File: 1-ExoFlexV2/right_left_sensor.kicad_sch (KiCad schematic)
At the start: 20 parts, among them U30 SN74LVC3G14DCUT_V2, U31 SN74LVC3G14DCUT_V2, U32 SN74LVC1G08DBVR, U33 SN74LVC3G14DCUT_V2, U34 SN74LVC3G14DCUT_V2, U35 SN74LVC1G08DBVR, U36 SN74LVC1G32DBVR

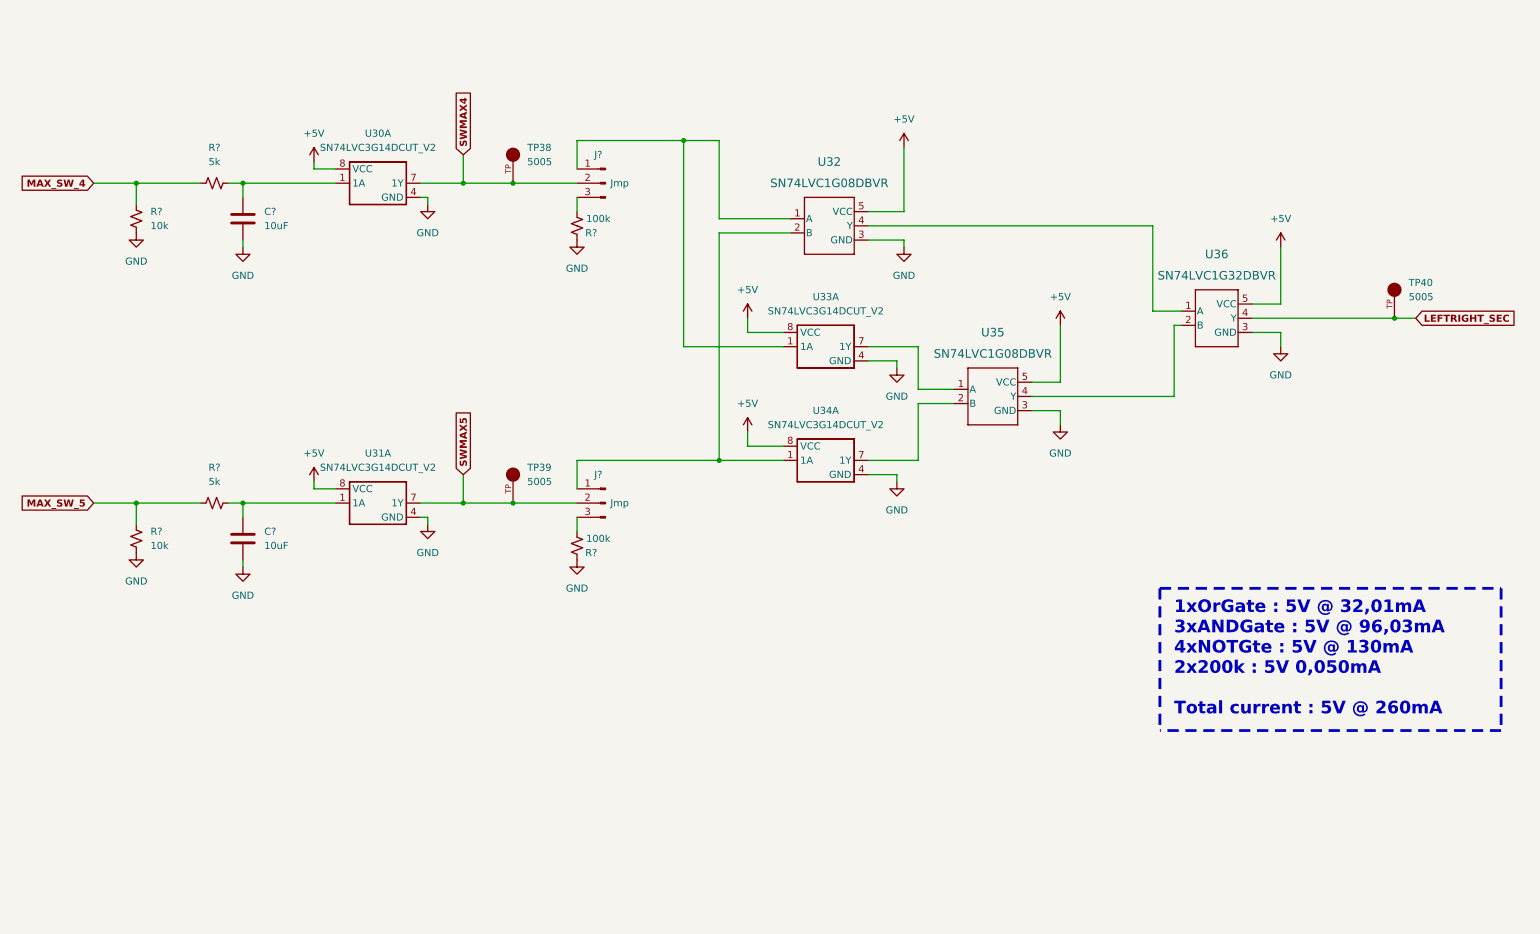
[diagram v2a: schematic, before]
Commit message: Test points et notes
- Ajout de tous les tests point nécessaires
-  Ajoute des sections de notes dans chaque page
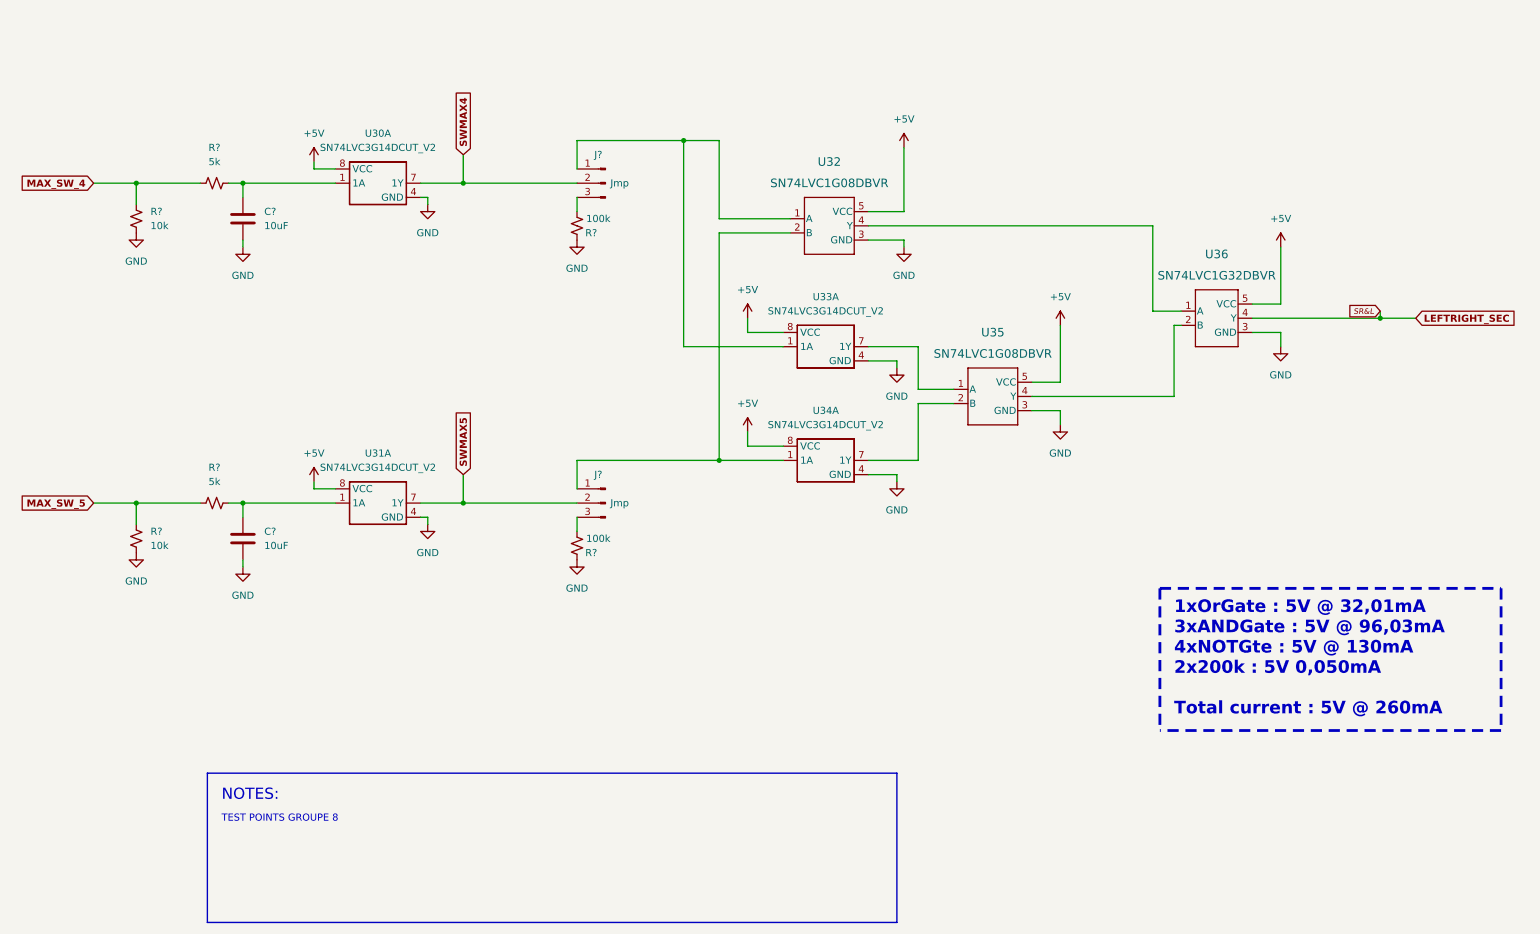
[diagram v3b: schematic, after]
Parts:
- removed TP38, TP39, TP40: 5005, FootPrint:KEYSTONE_5005, symbol SymLib:5005
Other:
- note added: "NOTES:"
- note added: "TEST POINTS GROUPE 8"
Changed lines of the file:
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@@
   (junction (at 96.52 120.65) (diameter 0) (color 0 0 0 0)
   )
-  (junction (at 105.41 63.5) (diameter 0) (color 0 0 0 0)
-  )
   (junction (at 38.1 63.5) (diameter 0) (color 0 0 0 0)
   )
-  (junction (at 262.89 87.63) (diameter 0) (color 0 0 0 0)
+  (junction (at 260.35 87.63) (diameter 0) (color 0 0 0 0)
   )
   (junction (at 135.89 55.88) (diameter 0) (color 0 0 0 0)
   )
-  (junction (at 105.41 120.65) (diameter 0) (color 0 0 0 0)
-  )
   (junction (at 38.1 120.65) (diameter 0) (color 0 0 0 0)
   )
@@
     (stroke (width 0) (type default) (color 0 0 0 0))
   )
-  (wire (pts (xy 96.52 120.65) (xy 105.41 120.65))
+  (wire (pts (xy 96.52 120.65) (xy 116.84 120.65))
     (stroke (width 0) (type default) (color 0 0 0 0))
   )
@@
     (stroke (width 0.5) (type dash) (color 255 148 44 1))
   )
+  (polyline (pts (xy 173.99 195.58) (xy 50.8 195.58))
+    (stroke (width 0.25) (type solid) (color 0 0 0 0))
+  )
   (wire (pts (xy 242.57 85.09) (xy 237.49 85.09))
     (stroke (width 0) (type default) (color 0 0 0 0))
@@
     (stroke (width 0) (type default) (color 0 0 0 0))
   )
-  (wire (pts (xy 105.41 120.65) (xy 116.84 120.65))
-    (stroke (width 0) (type default) (color 0 0 0 0))
-  )
   (wire (pts (xy 135.89 55.88) (xy 135.89 92.71))
     (stroke (width 0) (type default) (color 0 0 0 0))
   )
   (wire (pts (xy 57.15 130.81) (xy 57.15 132.08))
-    (stroke (width 0) (type default) (color 0 0 0 0))
-  )
-  (wire (pts (xy 105.41 63.5) (xy 116.84 63.5))
     (stroke (width 0) (type default) (color 0 0 0 0))
   )
@@
     (stroke (width 0.5) (type dash) (color 255 148 44 1))
   )
+  (polyline (pts (xy 50.8 168.91) (xy 50.8 195.58))
+    (stroke (width 0.25) (type solid) (color 0 0 0 0))
+  )
   (wire (pts (xy 90.17 67.31) (xy 90.17 66.04))
     (stroke (width 0) (type default) (color 0 0 0 0))
@@
     (stroke (width 0) (type default) (color 0 0 0 0))
   )
-  (wire (pts (xy 96.52 63.5) (xy 105.41 63.5))
+  (wire (pts (xy 96.52 63.5) (xy 116.84 63.5))
     (stroke (width 0) (type default) (color 0 0 0 0))
   )
@@
     (stroke (width 0) (type default) (color 0 0 0 0))
   )
+  (polyline (pts (xy 50.8 168.91) (xy 173.99 168.91))
+    (stroke (width 0.25) (type solid) (color 0 0 0 0))
+  )
   (wire (pts (xy 57.15 120.65) (xy 73.66 120.65))
     (stroke (width 0) (type default) (color 0 0 0 0))
@@
     (stroke (width 0) (type default) (color 0 0 0 0))
   )
+  (wire (pts (xy 260.35 86.36) (xy 260.35 87.63))
+    (stroke (width 0) (type default) (color 0 0 0 0))
+  )
   (wire (pts (xy 116.84 113.03) (xy 142.24 113.03))
     (stroke (width 0) (type default) (color 0 0 0 0))
@@
     (stroke (width 0) (type default) (color 0 0 0 0))
   )
+  (polyline (pts (xy 173.99 168.91) (xy 173.99 195.58))
+    (stroke (width 0.25) (type solid) (color 0 0 0 0))
+  )
   (wire (pts (xy 73.66 118.11) (xy 69.85 118.11))
     (stroke (width 0) (type default) (color 0 0 0 0))
   )
-  (wire (pts (xy 237.49 87.63) (xy 262.89 87.63))
+  (wire (pts (xy 237.49 87.63) (xy 260.35 87.63))
     (stroke (width 0) (type default) (color 0 0 0 0))
   )
@@
     (stroke (width 0) (type default) (color 0 0 0 0))
   )
-  (wire (pts (xy 262.89 87.63) (xy 266.7 87.63))
-    (stroke (width 0) (type default) (color 0 0 0 0))
+  (wire (pts (xy 260.35 87.63) (xy 266.7 87.63))
+    (stroke (width 0) (type default) (color 0 0 0 0))
+  )
+  (text "NOTES:" (at 53.34 173.99 0)
+    (effects (font (size 2 2)) (justify left bottom))
   )
   (text "1xOrGate : 5V @ 32,01mA\n3xANDGate : 5V @ 96,03mA\n4xNOTGte : 5V @ 130mA\n2x200k : 5V 0,050mA\n\nTotal current : 5V @ 260mA"
     (at 223.52 158.75 0)
     (effects (font (size 2.25 2.25) (thickness 0.5) bold) (justify left bottom))
+  )
+  (text "TEST POINTS GROUPE 8" (at 53.34 177.8 0)
+    (effects (font (size 1.27 1.27)) (justify left bottom))
   )
   (global_label "MAX_SW_5" (shape input) (at 30.48 120.65 180) (fields_autoplaced)
@@
     )
   )
+  (global_label "SR&L" (shape input) (at 260.35 86.36 180) (fields_autoplaced)
+    (effects (font (size 1 1) italic) (justify right))
+    (property "Intersheet References" "${INTERSHEET_REFS}" (id 0) (at 254.0987 86.2975 0)
+      (effects (font (size 1 1) italic) (justify right) hide)
+    )
+  )
   (global_label "SWMAX5" (shape input) (at 96.52 115.57 90) (fields_autoplaced)
     (effects (font (size 1.27 1.27) (thickness 0.254) bold) (justify left))
@@
     )
   )
-  (symbol (lib_id "SymLib:5005") (at 105.41 58.42 90) (unit 1)
-    (in_bom yes) (on_board yes) (fields_autoplaced)
-    (property "Reference" "TP38" (id 0) (at 107.95 57.1499 90)
-      (effects (font (size 1.27 1.27)) (justify right))
-    )
-    (property "Value" "5005" (id 1) (at 107.95 59.6899 90)
-      (effects (font (size 1.27 1.27)) (justify right))
-    )
-    (property "Footprint" "FootPrint:KEYSTONE_5005" (id 2) (at 105.41 58.42 0)
-      (effects (font (size 1.27 1.27)) (justify bottom) hide)
-    )
-    (property "Datasheet" "" (id 3) (at 105.41 58.42 0)
-      (effects (font (size 1.27 1.27)) hide)
-    )
-    (property "MF" "Keystone Electronics" (id 4) (at 105.41 58.42 0)
-      (effects (font (size 1.27 1.27)) (justify bottom) hide)
-    )
-    (property "DESCRIPTION" "Compact THM Test Point -Red" (id 5) (at 105.41 58.42 0)
-      (effects (font (size 1.27 1.27)) (justify bottom) hide)
-    )
-    (property "PACKAGE" "NON STANDARD-1 Keystone" (id 6) (at 105.41 58.42 0)
-      (effects (font (size 1.27 1.27)) (justify bottom) hide)
-    )
-    (property "PRICE" "None" (id 7) (at 105.41 58.42 0)
-      (effects (font (size 1.27 1.27)) (justify bottom) hide)
-    )
-    (property "MP" "5005" (id 8) (at 105.41 58.42 0)
-      (effects (font (size 1.27 1.27)) (justify bottom) hide)
-    )
-    (property "AVAILABILITY" "In Stock" (id 9) (at 105.41 58.42 0)
-      (effects (font (size 1.27 1.27)) (justify bottom) hide)
-    )
-    (property "PURCHASE-URL" "https://pricing.snapeda.com/search/part/5005/?ref=eda" (id 10) (at 105.41 58.42 0)
-      (effects (font (size 1.27 1.27)) (justify bottom) hide)
-    )
-    (pin "TP")
-  )
   (symbol (lib_id "Device:C") (at 57.15 127 0) (unit 1)
     (in_bom yes) (on_board yes) (fields_autoplaced)
@@
     )
     (pin "1")
-  )
-  (symbol (lib_id "SymLib:5005") (at 105.41 115.57 90) (unit 1)
-    (in_bom yes) (on_board yes) (fields_autoplaced)
-    (property "Reference" "TP39" (id 0) (at 107.95 114.2999 90)
-      (effects (font (size 1.27 1.27)) (justify right))
-    )
-    (property "Value" "5005" (id 1) (at 107.95 116.8399 90)
-      (effects (font (size 1.27 1.27)) (justify right))
-    )
-    (property "Footprint" "FootPrint:KEYSTONE_5005" (id 2) (at 105.41 115.57 0)
-      (effects (font (size 1.27 1.27)) (justify bottom) hide)
-    )
-    (property "Datasheet" "" (id 3) (at 105.41 115.57 0)
-      (effects (font (size 1.27 1.27)) hide)
-    )
-    (property "MF" "Keystone Electronics" (id 4) (at 105.41 115.57 0)
-      (effects (font (size 1.27 1.27)) (justify bottom) hide)
-    )
-    (property "DESCRIPTION" "Compact THM Test Point -Red" (id 5) (at 105.41 115.57 0)
-      (effects (font (size 1.27 1.27)) (justify bottom) hide)
-    )
-    (property "PACKAGE" "NON STANDARD-1 Keystone" (id 6) (at 105.41 115.57 0)
-      (effects (font (size 1.27 1.27)) (justify bottom) hide)
-    )
-    (property "PRICE" "None" (id 7) (at 105.41 115.57 0)
-      (effects (font (size 1.27 1.27)) (justify bottom) hide)
-    )
-    (property "MP" "5005" (id 8) (at 105.41 115.57 0)
-      (effects (font (size 1.27 1.27)) (justify bottom) hide)
-    )
-    (property "AVAILABILITY" "In Stock" (id 9) (at 105.41 115.57 0)
-      (effects (font (size 1.27 1.27)) (justify bottom) hide)
-    )
-    (property "PURCHASE-URL" "https://pricing.snapeda.com/search/part/5005/?ref=eda" (id 10) (at 105.41 115.57 0)
-      (effects (font (size 1.27 1.27)) (justify bottom) hide)
-    )
-    (pin "TP")
   )
   (symbol (lib_id "SymLib:SN74LVC1G08DBVR") (at 137.16 68.58 0) (unit 1)
@@
     (pin "2")
   )
-  (symbol (lib_id "SymLib:5005") (at 262.89 82.55 90) (unit 1)
-    (in_bom yes) (on_board yes) (fields_autoplaced)
-    (property "Reference" "TP40" (id 0) (at 265.43 81.2799 90)
-      (effects (font (size 1.27 1.27)) (justify right))
-    )
-    (property "Value" "5005" (id 1) (at 265.43 83.8199 90)
-      (effects (font (size 1.27 1.27)) (justify right))
-    )
-    (property "Footprint" "FootPrint:KEYSTONE_5005" (id 2) (at 262.89 82.55 0)
-      (effects (font (size 1.27 1.27)) (justify bottom) hide)
-    )
-    (property "Datasheet" "" (id 3) (at 262.89 82.55 0)
-      (effects (font (size 1.27 1.27)) hide)
-    )
-    (property "MF" "Keystone Electronics" (id 4) (at 262.89 82.55 0)
-      (effects (font (size 1.27 1.27)) (justify bottom) hide)
-    )
-    (property "DESCRIPTION" "Compact THM Test Point -Red" (id 5) (at 262.89 82.55 0)
-      (effects (font (size 1.27 1.27)) (justify bottom) hide)
-    )
-    (property "PACKAGE" "NON STANDARD-1 Keystone" (id 6) (at 262.89 82.55 0)
-      (effects (font (size 1.27 1.27)) (justify bottom) hide)
-    )
-    (property "PRICE" "None" (id 7) (at 262.89 82.55 0)
-      (effects (font (size 1.27 1.27)) (justify bottom) hide)
-    )
-    (property "MP" "5005" (id 8) (at 262.89 82.55 0)
-      (effects (font (size 1.27 1.27)) (justify bottom) hide)
-    )
-    (property "AVAILABILITY" "In Stock" (id 9) (at 262.89 82.55 0)
-      (effects (font (size 1.27 1.27)) (justify bottom) hide)
-    )
-    (property "PURCHASE-URL" "https://pricing.snapeda.com/search/part/5005/?ref=eda" (id 10) (at 262.89 82.55 0)
-      (effects (font (size 1.27 1.27)) (justify bottom) hide)
-    )
-    (pin "TP")
-  )
   (symbol (lib_id "Device:R_Small_US") (at 52.07 120.65 90) (unit 1)

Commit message: Schématisation terminée
- Schéma terminé
- Passage vers le PCB
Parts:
- C35, C36: renamed from C?; value 10uF -> 10uF 10V X7R; DESCRIPTION (none) -> 10 µF ±10% 10V Ceramic Capacitor X7R 0805 (2012 Metric); MANUFACTURER (none) -> Murata Electronics; PACKAGE (none) -> 0805 (2012 Metric); PART NUMBER (none) -> GRM21BR71A106KA73L; TYPE (none) -> SMD
- J92, J93: renamed from J?; value Jmp -> Jumper; footprint (none) -> Connector_PinSocket_2.54mm:PinSocket_1x03_P2.54mm_Vertical; DESCRIPTION (none) -> CONN HEADER VERT 3POS 2.54MM; MANUFACTURER (none) -> Würth Elektronik; PACKAGE (none) -> Square 0.100" (2.54mm); PART NUMBER (none) -> 61300311121; TYPE (none) -> Through Hole
- R115, R116: renamed from R?; value 10k -> 10k 5% 1/8W; DESCRIPTION (none) -> 10 kOhms ±5% 0.125W, 1/8W Chip Resistor 0805 (2012 Metric) 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; MANUFACTURER (none) -> Panasonic Electronic Components; PACKAGE (none) -> 0805 (2012 Metric); PART NUMBER (none) -> ERJ-6GEYJ103V; TYPE (none) -> SMD
- R117, R118: renamed from R?; value 5k -> 5,1k 5% 1/8W; DESCRIPTION (none) -> 5.1 kOhms ±5% 0.125W, 1/8W Chip Resistor 0805 (2012 Metric)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; MANUFACTURER (none) -> Panasonic Electronic Components; PACKAGE (none) -> 0805 (2012 Metric); PART NUMBER (none) -> ERJ-6GEYJ512V; TYPE (none) -> SMD
- R119, R120: renamed from R?; value 100k -> 100k 5% 1/8W; DESCRIPTION (none) -> 100 kOhms ±5% 0.125W, 1/8W Chip Resistor 0805 (2012 Metric)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; MANUFACTURER (none) -> Panasonic Electronic Components; PACKAGE (none) -> 0805 (2012 Metric); PART NUMBER (none) -> ERJ-6GEYJ104V; TYPE (none) -> SMD
- U51: renamed from U30; value SN74LVC3G14DCUT_V2 -> Inverter; DESCRIPTION (none) -> Inverter IC 3 Channel Schmitt Trigger 8-VSSOP; MANUFACTURER (none) -> Texas Instruments; PACKAGE (none) -> 8-VFSOP (0.091", 2.30mm Width); PART NUMBER (none) -> SN74LVC3G14DCUT; TYPE (none) -> SMD
- U52: renamed from U31; value SN74LVC3G14DCUT_V2 -> Inverter; DESCRIPTION (none) -> Inverter IC 3 Channel Schmitt Trigger 8-VSSOP; MANUFACTURER (none) -> Texas Instruments; PACKAGE (none) -> 8-VFSOP (0.091", 2.30mm Width); PART NUMBER (none) -> SN74LVC3G14DCUT; TYPE (none) -> SMD
- U53: renamed from U32; value SN74LVC1G08DBVR -> AND Gate; DESCRIPTION (none) -> AND Gate IC 1 Channel SOT-23-5; MANUFACTURER (none) -> Texas Instruments; PACKAGE (none) -> SC-74A, SOT-753; PART NUMBER (none) -> SN74LVC1G08DBVR; TYPE (none) -> SMD
- U54: renamed from U33; value SN74LVC3G14DCUT_V2 -> Inverter; DESCRIPTION (none) -> Inverter IC 3 Channel Schmitt Trigger 8-VSSOP; MANUFACTURER (none) -> Texas Instruments; PACKAGE (none) -> 8-VFSOP (0.091", 2.30mm Width); PART NUMBER (none) -> SN74LVC3G14DCUT; TYPE (none) -> SMD
- U55: renamed from U34; value SN74LVC3G14DCUT_V2 -> Inverter; DESCRIPTION (none) -> Inverter IC 3 Channel Schmitt Trigger 8-VSSOP; MANUFACTURER (none) -> Texas Instruments; PACKAGE (none) -> 8-VFSOP (0.091", 2.30mm Width); PART NUMBER (none) -> SN74LVC3G14DCUT; TYPE (none) -> SMD
- U56: renamed from U35; value SN74LVC1G08DBVR -> AND Gate; DESCRIPTION (none) -> AND Gate IC 1 Channel SOT-23-5; MANUFACTURER (none) -> Texas Instruments; PACKAGE (none) -> SC-74A, SOT-753; PART NUMBER (none) -> SN74LVC1G08DBVR; TYPE (none) -> SMD
- U57: renamed from U36; value SN74LVC1G32DBVR -> OR Gate; DESCRIPTION (none) -> OR Gate IC 1 Channel SOT-23-5; MANUFACTURER (none) -> Texas Instruments; PACKAGE (none) -> SC-74A, SOT-753; PART NUMBER (none) -> SN74LVC1G32DBVR; TYPE (none) -> SMD
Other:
- note added: "1xOrGate : 5V @ 32,01mA 3xANDGate : 5V @ 96,03mA 4xNOTGte : 5V @ 130mA 2x100k : 5V 0,1mA Total current : 5V @ 261mA"
- note removed: "1xOrGate : 5V @ 32,01mA 3xANDGate : 5V @ 96,03mA 4xNOTGte : 5V @ 130mA 2x200k : 5V 0,050mA Total current : 5V @ 260mA"
